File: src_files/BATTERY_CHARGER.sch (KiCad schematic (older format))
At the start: 13 parts, among them Q11 IRFR9024NTRPBF, U21 SY6912A

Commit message: updated footprint and schematics
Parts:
- added C149, C150, C283: 22uF, Capacitor_SMD:C_0402_1005Metric, symbol Device:C_Small
- added D1: SS56, greencharge-footprints:SMAG, symbol Device:D
- added L15: 470nH, symbol Device:L
- added R28: 100K, Resistor_SMD:R_0402_1005Metric, symbol Device:R_US
- added R29: 806K, Resistor_SMD:R_0402_1005Metric, symbol Device:R_US
- added R30: 91K, Resistor_SMD:R_0402_1005Metric, symbol Device:R_US
- added U7: TPS63802DLAR, greencharge-footprints:VREG_TPS63802DLAR, symbol TPS63802DLAR:TPS63802DLAR
- C251: value 130pF -> 3200pF; MPN CC0603JRNPO9BN131 -> 06031C322KAT2A
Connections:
- net +5V: now also D1.1 (K)
- net GND: now also C149.2, C150.2, C283.2, R30.2, U7.2 (MODE), U7.3 (AGND), U7.8 (GND)
- net VBAT: now also C149.1, U7.1 (EN), U7.10 (VIN)
- new net: R28.2, U7.5 (PG)
- new net: C150.1, C283.1, D1.2 (A), R28.1, R29.1, U7.6 (VOUT)
- new net: L15.1, U7.7 (L2)
- new net: L15.2, U7.9 (L1)
- new net FB: R29.2, R30.1, U7.4 (FB)
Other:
- note added: "1A output charging current for best life cycle"
- note added: "BAT CHARGER SECTION"
- note added: "Ctim=16,200‬(4.0Hrs)\nformula=\nCTIM=2*10-11TCC\n"
- note added: "REVERSE CURRENT/VOLTAGE BLOCKING DIODE"
- note added: "THIS BAT SOURCE CAN ONLY SUPPLY 2A MAX VIA THE 3.3V RAIL\n\n"
- note added: "V_BAT TO 5V(2A) BOOTS IC"
- note removed: "THIS BAT SOURCE CAN ONLY SUPPLY 2A MAX VIA THE 3.3V RAIL\n5V SOURCES ARE THUS NOT SUPPLIED(TO BE ACCERTAINED IF NEEDED)\n"
- moved on the sheet: C251

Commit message: complete update on schematiC + FOOTPRINT
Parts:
- L15: footprint (none) -> greencharge-footprints:FNR4018SR47NT
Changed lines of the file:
@@
 F 0 "L15" H 2732 5179 50  0000 R CNN
 F 1 "470nH" H 2732 5270 50  0000 R CNN
-F 2 "" H 2775 5225 50  0001 C CNN
+F 2 "greencharge-footprints:FNR4018SR47NT" H 2775 5225 50  0001 C CNN
 F 3 "~" H 2775 5225 50  0001 C CNN
 F 4 "4A_±30%_18m_Ohm" H 2775 5225 50  0001 C CNN "Description"

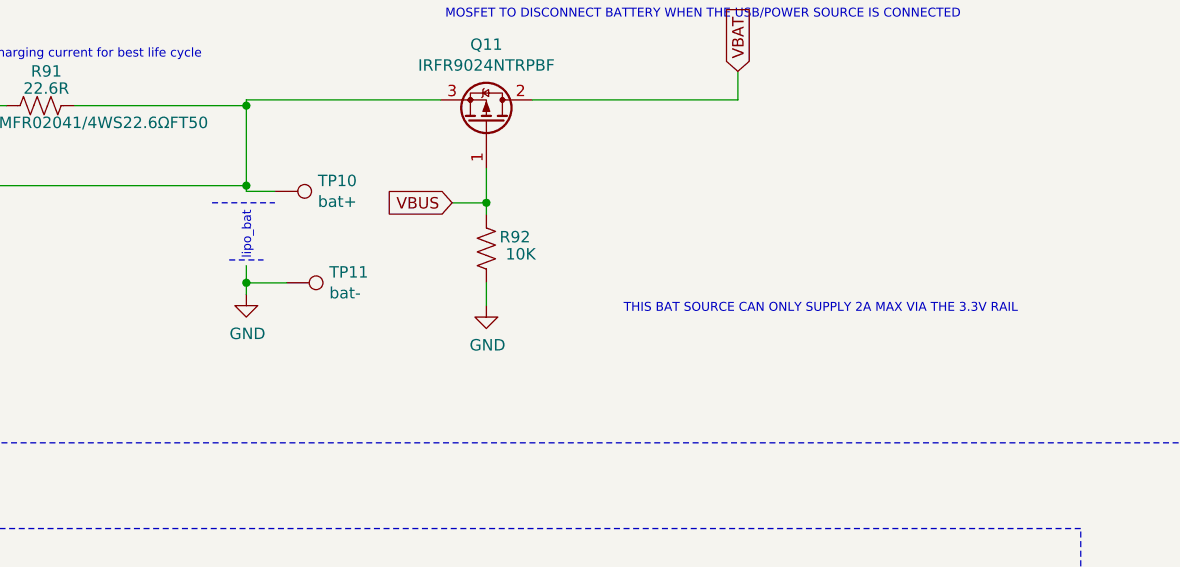
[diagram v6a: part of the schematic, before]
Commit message: updates rules check and associations
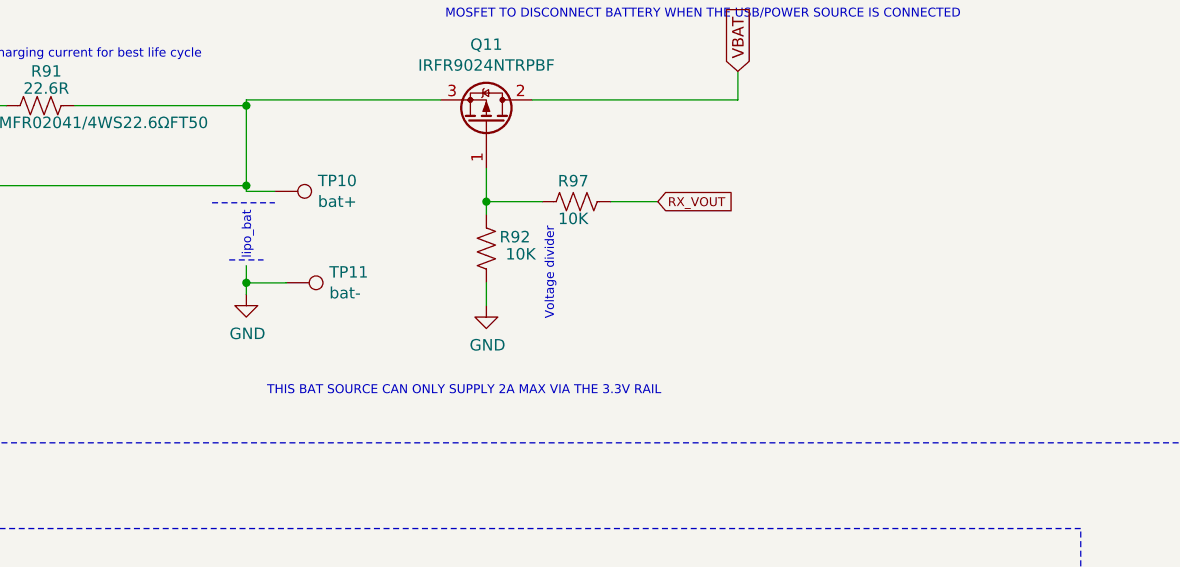
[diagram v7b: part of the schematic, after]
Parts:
- added R97: 10K, Resistor_SMD:R_0402_1005Metric, symbol Device:R_US
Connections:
- net VBUS: no longer names the net of Q11.1 (G), R92.1
- net VBUS: now also R97.1
- new net RX_VOUT: R97.2
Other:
- note added: "Voltage divider"
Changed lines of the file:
@@
 Connection ~ 2450 1175
 Connection ~ 5825 2000
-Text GLabel 6725 2425 0    50   Input ~ 0
-VBUS
 Text Notes 8950 1625 2    39   ~ 0
 MOSFET TO DISCONNECT BATTERY WHEN THE USB/POWER SOURCE IS CONNECTED
@@
 	6875 2875 6875 2775
 Wire Wire Line
-	6875 2475 6875 2425
-Wire Wire Line
-	6725 2425 6875 2425
-Connection ~ 6875 2425
-Wire Wire Line
-	6875 2425 6875 2275
-Wire Wire Line
 	7975 1850 7975 1975
-Text Notes 9200 2975 2    39   ~ 0
+Text Notes 7640 3335 2    39   ~ 0
 THIS BAT SOURCE CAN ONLY SUPPLY 2A MAX VIA THE 3.3V RAIL\n\n
 $Comp
@@
 Wire Notes Line
 	9475 3850 4400 3850
+Text GLabel 7625 2420 2    39   Input ~ 0
+RX_VOUT
+$Comp
+L Device:R_US R?
+U 1 1 63F2463D
+P 7270 2420
+AR Path="/63F2463D" Ref="R?"  Part="1"
+AR Path="/672F9255/63F2463D" Ref="R97"  Part="1"
+F 0 "R97" V 7360 2435 50  0000 C CNN
+F 1 "10K" V 7195 2435 50  0000 C CNN
+F 2 "Resistor_SMD:R_0402_1005Metric" V 7310 2410 50  0001 C CNN
+F 3 "~" H 7270 2420 50  0001 C CNN
+	1    7270 2420
+	0    -1   -1   0
+$EndComp
+Wire Wire Line
+	7625 2420 7420 2420
+Wire Wire Line
+	6875 2275 6875 2420
+Connection ~ 6875 2420
+Wire Wire Line
+	6875 2420 6875 2475
+Wire Wire Line
+	7120 2420 6875 2420
+Text Notes 7175 2940 1    39   ~ 0
+Voltage divider
 $EndSCHEMATC
